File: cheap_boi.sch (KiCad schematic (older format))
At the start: 120 parts, among them SW1 SW_Push, U1 ATmega32U4-AU, Y1 16MHz

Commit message: assigned footprints for all components
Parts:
- MX0, MX0A1, MX0B1, MX0C1, MX1, MX10, MX11, MX12, MX13, MX14, MX15, MX16, MX17, MX18, MX19, MX1A1, MX1B1, MX1C1, MX2, MX20, MX21, MX22, MX23, MX24, MX25, MX26, MX27, MX28, MX29, MX2A1, MX2B1, MX2C1, MX3, MX30, MX31, MX32, MX33, MX34, MX35, MX36, MX37, MX38, MX39, MX3A1, MX3B1, MX3C1, MX4, MX5, MX6, MX7, MX8, MX9: footprint (none) -> MX_Alps_Hybrid_2:MX-1U-NoLED
- R1, R2, R3, R4: footprint (none) -> Resistor_SMD:R_0805_2012Metric
- SW1: footprint (none) -> random-keyboard-parts:SKQG-1155865
- USB1: footprint (none) -> random-keyboard-parts:Molex-0548190589
- Y1: footprint (none) -> Crystal:Crystal_SMD_3225-4Pin_3.2x2.5mm

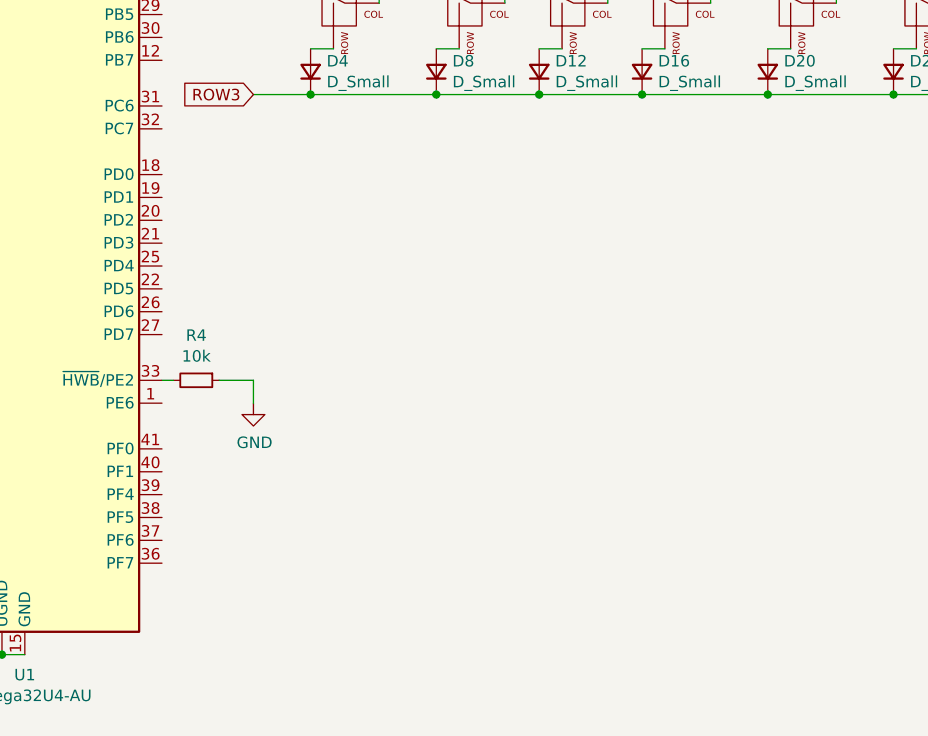
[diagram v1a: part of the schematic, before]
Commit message: added RGB breakout and ordered parts in symmetrically
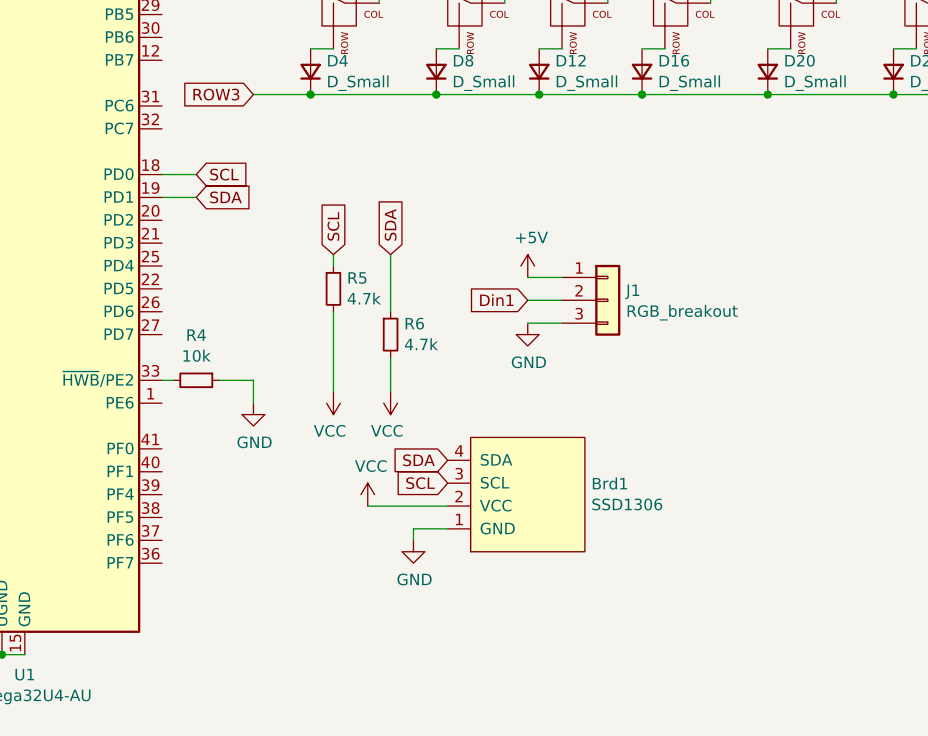
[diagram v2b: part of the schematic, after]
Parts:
- added Brd1: SSD1306, SSD1306:128x64OLED, symbol SSD1306-128x64_OLED:SSD1306
- added J1: RGB_breakout, Connector_PinHeader_1.00mm:PinHeader_1x03_P1.00mm_Vertical_SMD_Pin1Left, symbol Connector_Generic:Conn_01x03
- added R5, R6: 4.7k, Resistor_SMD:R_0805_2012Metric, symbol Device:R_Small
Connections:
- net +5V: now also J1.1 (Pin_1)
- net GND: now also Brd1.1 (GND), J1.3 (Pin_3)
- net VCC: now also Brd1.2 (VCC), R5.2, R6.2
- net SCL: now reaches U1.18 (PD0)
- net SCL: now also Brd1.3 (SCL), R5.1
- net SDA: now reaches U1.19 (PD1)
- net SDA: now also Brd1.4 (SDA), R6.1
- new net Din1: J1.2 (Pin_2)
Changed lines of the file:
@@
 	1    0    0    -1
 $EndComp
+Text GLabel 3400 4900 2    50   Input ~ 0
+SDA
+Text GLabel 3400 4800 2    50   Input ~ 0
+SCL
+Wire Wire Line
+	3250 4800 3400 4800
+Wire Wire Line
+	3400 4900 3250 4900
+$Comp
+L SSD1306-128x64_OLED:SSD1306 Brd1
+U 1 1 5EFF64F3
+P 4850 6200
+F 0 "Brd1" V 4896 5922 50  0000 R CNN
+F 1 "SSD1306" V 4805 5922 50  0000 R CNN
+F 2 "SSD1306:128x64OLED" H 4850 6450 50  0001 C CNN
+F 3 "" H 4850 6450 50  0001 C CNN
+	1    4850 6200
+	0    -1   -1   0
+$EndComp
+Text GLabel 4500 6150 0    50   Input ~ 0
+SCL
+Text GLabel 4500 6050 0    50   Input ~ 0
+SDA
+$Comp
+L power:GND #PWR0114
+U 1 1 5F0207B3
+P 4350 6400
+F 0 "#PWR0114" H 4350 6150 50  0001 C CNN
+F 1 "GND" H 4355 6227 50  0000 C CNN
+F 2 "" H 4350 6400 50  0001 C CNN
+F 3 "" H 4350 6400 50  0001 C CNN
+	1    4350 6400
+	1    0    0    -1
+$EndComp
+Wire Wire Line
+	4500 6350 4350 6350
+Wire Wire Line
+	4350 6350 4350 6400
+Wire Wire Line
+	4500 6250 4150 6250
+$Comp
+L power:VCC #PWR0115
+U 1 1 5F08A572
+P 4150 6250
+F 0 "#PWR0115" H 4150 6100 50  0001 C CNN
+F 1 "VCC" H 4165 6423 50  0000 C CNN
+F 2 "" H 4150 6250 50  0001 C CNN
+F 3 "" H 4150 6250 50  0001 C CNN
+	1    4150 6250
+	1    0    0    -1
+$EndComp
+Text GLabel 4000 5150 1    50   Input ~ 0
+SCL
+Text GLabel 4250 5150 1    50   Input ~ 0
+SDA
+$Comp
+L Device:R_Small R5
+U 1 1 5F0A18D6
+P 4000 5300
+F 0 "R5" H 4059 5346 50  0000 L CNN
+F 1 "4.7k" H 4059 5255 50  0000 L CNN
+F 2 "Resistor_SMD:R_0805_2012Metric" H 4000 5300 50  0001 C CNN
+F 3 "~" H 4000 5300 50  0001 C CNN
+	1    4000 5300
+	1    0    0    -1
+$EndComp
+$Comp
+L Device:R_Small R6
+U 1 1 5F0A2642
+P 4250 5500
+F 0 "R6" H 4309 5546 50  0000 L CNN
+F 1 "4.7k" H 4309 5455 50  0000 L CNN
+F 2 "Resistor_SMD:R_0805_2012Metric" H 4250 5500 50  0001 C CNN
+F 3 "~" H 4250 5500 50  0001 C CNN
+	1    4250 5500
+	1    0    0    -1
+$EndComp
+Wire Wire Line
+	4250 5150 4250 5400
+Wire Wire Line
+	4000 5150 4000 5200
+$Comp
+L power:VCC #PWR0116
+U 1 1 5F0D2F2C
+P 4250 5750
+F 0 "#PWR0116" H 4250 5600 50  0001 C CNN
+F 1 "VCC" H 4265 5923 50  0000 C CNN
+F 2 "" H 4250 5750 50  0001 C CNN
+F 3 "" H 4250 5750 50  0001 C CNN
+	1    4250 5750
+	-1   0    0    1
+$EndComp
+$Comp
+L power:VCC #PWR0117
+U 1 1 5F0D3517
+P 4000 5750
+F 0 "#PWR0117" H 4000 5600 50  0001 C CNN
+F 1 "VCC" H 4015 5923 50  0000 C CNN
+F 2 "" H 4000 5750 50  0001 C CNN
+F 3 "" H 4000 5750 50  0001 C CNN
+	1    4000 5750
+	-1   0    0    1
+$EndComp
+Wire Wire Line
+	4250 5600 4250 5750
+Wire Wire Line
+	4000 5400 4000 5750
+$Comp
+L Connector_Generic:Conn_01x03 J1
+U 1 1 5EF82DD1
+P 5200 5350
+F 0 "J1" H 5280 5392 50  0000 L CNN
+F 1 "RGB_breakout" H 5280 5301 50  0000 L CNN
+F 2 "Connector_PinHeader_1.00mm:PinHeader_1x03_P1.00mm_Vertical_SMD_Pin1Left" H 5200 5350 50  0001 C CNN
+F 3 "~" H 5200 5350 50  0001 C CNN
+	1    5200 5350
+	1    0    0    -1
+$EndComp
+$Comp
+L power:GND #PWR0118
+U 1 1 5F001636
+P 4850 5450
+F 0 "#PWR0118" H 4850 5200 50  0001 C CNN
+F 1 "GND" H 4855 5277 50  0000 C CNN
+F 2 "" H 4850 5450 50  0001 C CNN
+F 3 "" H 4850 5450 50  0001 C CNN
+	1    4850 5450
+	1    0    0    -1
+$EndComp
+$Comp
+L power:+5V #PWR0119
+U 1 1 5F00271B
+P 4850 5250
+F 0 "#PWR0119" H 4850 5100 50  0001 C CNN
+F 1 "+5V" H 4865 5423 50  0000 C CNN
+F 2 "" H 4850 5250 50  0001 C CNN
+F 3 "" H 4850 5250 50  0001 C CNN
+	1    4850 5250
+	1    0    0    -1
+$EndComp
+Text GLabel 4850 5350 0    50   Input ~ 0
+Din1
+Wire Wire Line
+	4850 5250 5000 5250
+Wire Wire Line
+	4850 5350 5000 5350
+Wire Wire Line
+	4850 5450 5000 5450
 $EndSCHEMATC

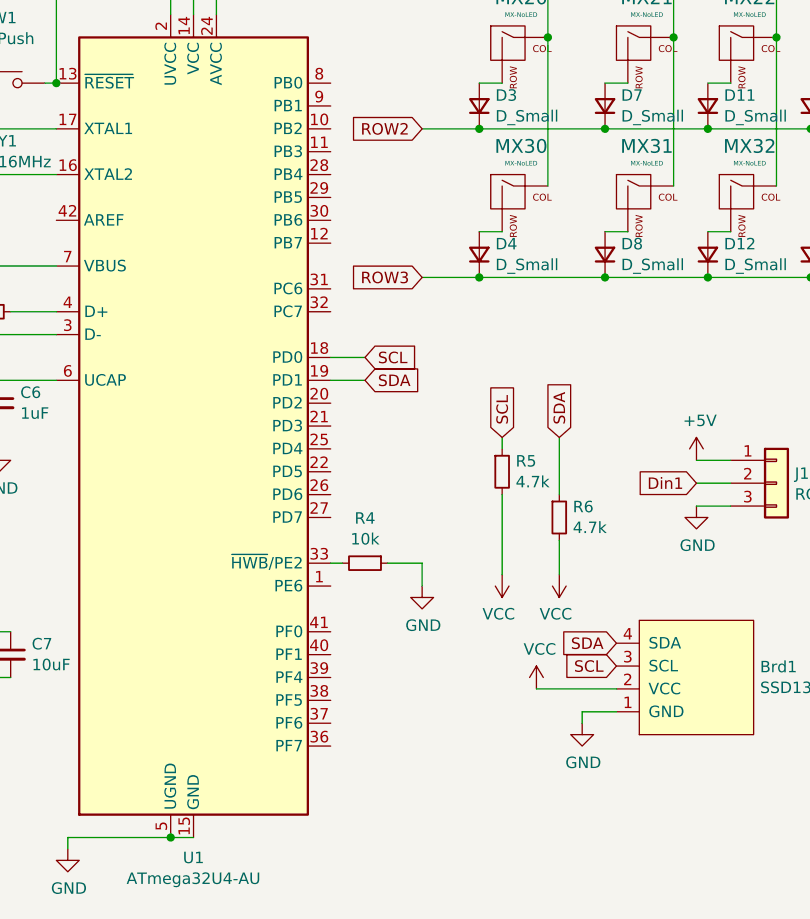
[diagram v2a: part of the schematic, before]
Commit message: added connection of rows and cols to microcontroller
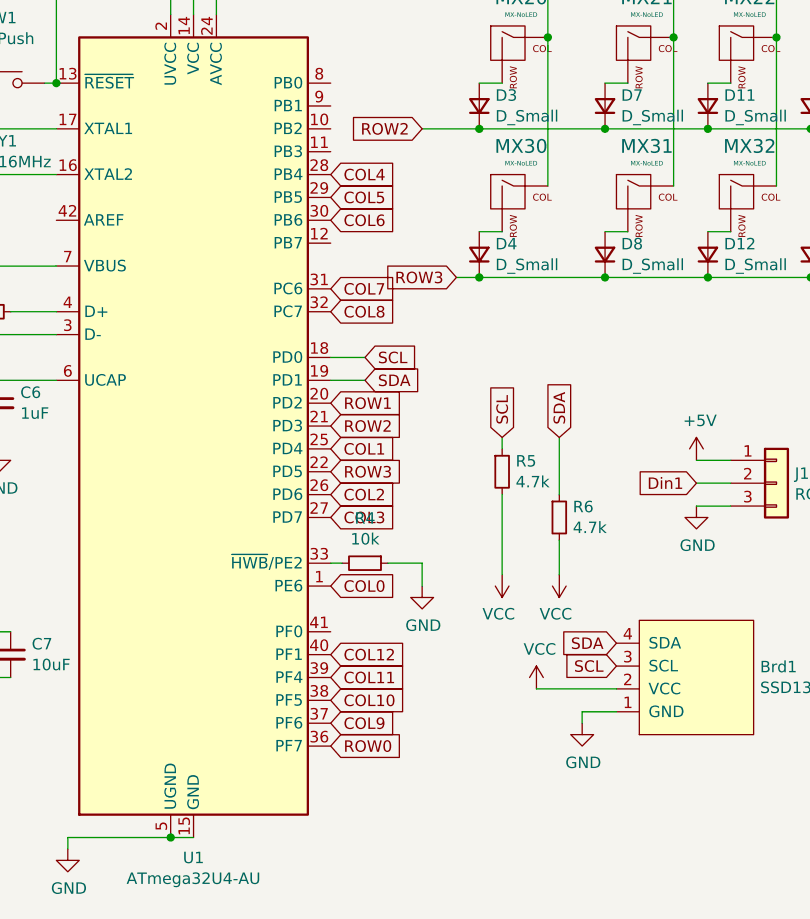
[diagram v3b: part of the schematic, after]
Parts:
- J1: footprint Connector_PinHeader_1.00mm:PinHeader_1x03_P1.00mm_Vertical_SMD_Pin1Left -> Connector_PinHeader_1.00mm:PinHeader_1x03_P1.00mm_Vertical
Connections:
- net COL0: now also U1.1 (PE6)
- net COL1: now also U1.25 (PD4)
- net COL10: now also U1.38 (PF5)
- net COL11: now also U1.39 (PF4)
- net COL12: now also U1.40 (PF1)
- net COL2: now also U1.26 (PD6)
- net COL3: now also U1.27 (PD7)
- net COL4: now also U1.28 (PB4)
- net COL5: now also U1.29 (PB5)
- net COL6: now also U1.30 (PB6)
- net COL7: now also U1.31 (PC6)
- net COL8: now also U1.32 (PC7)
- net COL9: now also U1.37 (PF6)
- net ROW0: now also U1.36 (PF7)
- net ROW1: now also U1.20 (PD2)
- net ROW2: now also U1.21 (PD3)
- net ROW3: now also U1.22 (PD5)
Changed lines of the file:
@@
 Connection ~ 3900 4450
 Wire Wire Line
-	3900 4450 3650 4450
+	3900 4450 3800 4450
 Connection ~ 4450 4450
 Wire Wire Line
@@
 Text GLabel 3650 3800 0    50   Input ~ 0
 ROW2
-Text GLabel 3650 4450 0    50   Input ~ 0
+Text GLabel 3800 4450 0    50   Input ~ 0
 ROW3
 Wire Wire Line
@@
 F 0 "#PWR0116" H 4250 5600 50  0001 C CNN
 F 1 "VCC" H 4265 5923 50  0000 C CNN
-F 2 "" H 4250 5750 50  0001 C CNN
+F 2 "COL6" H 4250 5750 50  0001 C CNN
 F 3 "" H 4250 5750 50  0001 C CNN
 	1    4250 5750
@@
 F 0 "J1" H 5280 5392 50  0000 L CNN
 F 1 "RGB_breakout" H 5280 5301 50  0000 L CNN
-F 2 "Connector_PinHeader_1.00mm:PinHeader_1x03_P1.00mm_Vertical_SMD_Pin1Left" H 5200 5350 50  0001 C CNN
+F 2 "Connector_PinHeader_1.00mm:PinHeader_1x03_P1.00mm_Vertical" H 5200 5350 50  0001 C CNN
 F 3 "~" H 5200 5350 50  0001 C CNN
 	1    5200 5350
@@
 Wire Wire Line
 	4850 5450 5000 5450
+Text GLabel 3250 6500 2    50   Input ~ 0
+ROW0
+Text GLabel 3250 5000 2    50   Input ~ 0
+ROW1
+Text GLabel 3250 5100 2    50   Input ~ 0
+ROW2
+Text GLabel 3250 5300 2    50   Input ~ 0
+ROW3
+Text GLabel 3250 5800 2    50   Input ~ 0
+COL0
+Text GLabel 3250 5200 2    50   Input ~ 0
+COL1
+Text GLabel 3250 5400 2    50   Input ~ 0
+COL2
+Text GLabel 3250 5500 2    50   Input ~ 0
+COL3
+Text GLabel 3250 4000 2    50   Input ~ 0
+COL4
+Text GLabel 3250 4100 2    50   Input ~ 0
+COL5
+Text GLabel 3250 4200 2    50   Input ~ 0
+COL6
+Text GLabel 3250 4500 2    50   Input ~ 0
+COL7
+Text GLabel 3250 4600 2    50   Input ~ 0
+COL8
+Text GLabel 3250 6400 2    50   Input ~ 0
+COL9
+Text GLabel 3250 6300 2    50   Input ~ 0
+COL10
+Text GLabel 3250 6200 2    50   Input ~ 0
+COL11
+Text GLabel 3250 6100 2    50   Input ~ 0
+COL12
 $EndSCHEMATC

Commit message: tracing is done, PCB should be functional
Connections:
- net Din1: now also U1.8 (PB0)
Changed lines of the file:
@@
 Text GLabel 3250 6100 2    50   Input ~ 0
 COL12
+Text GLabel 3250 3600 2    50   Input ~ 0
+Din1
 $EndSCHEMATC

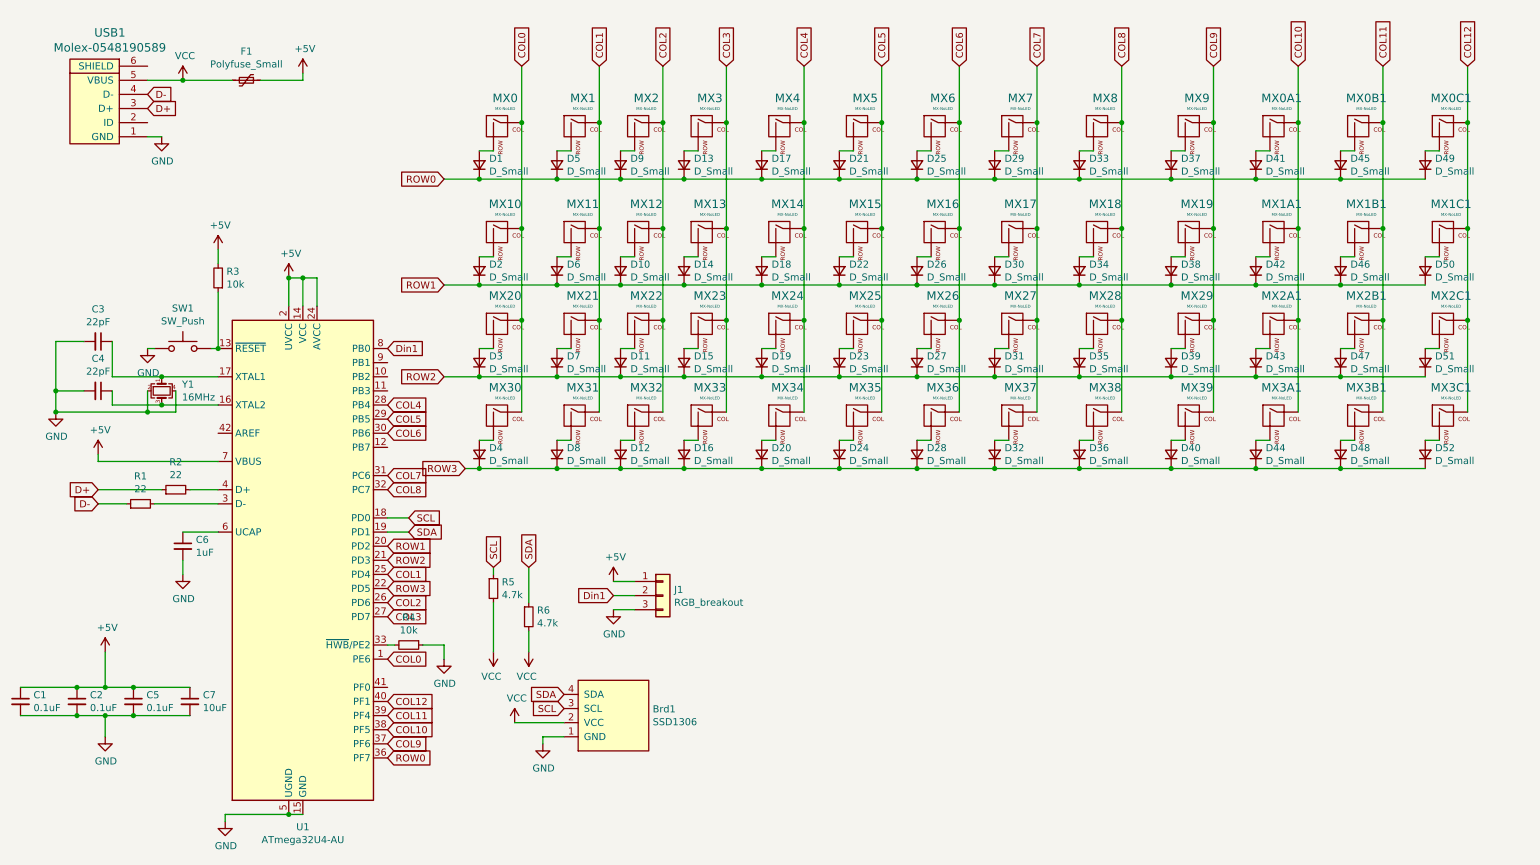
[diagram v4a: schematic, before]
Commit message: added RGB underglow, removed 3 pin breakout for RGB underglow
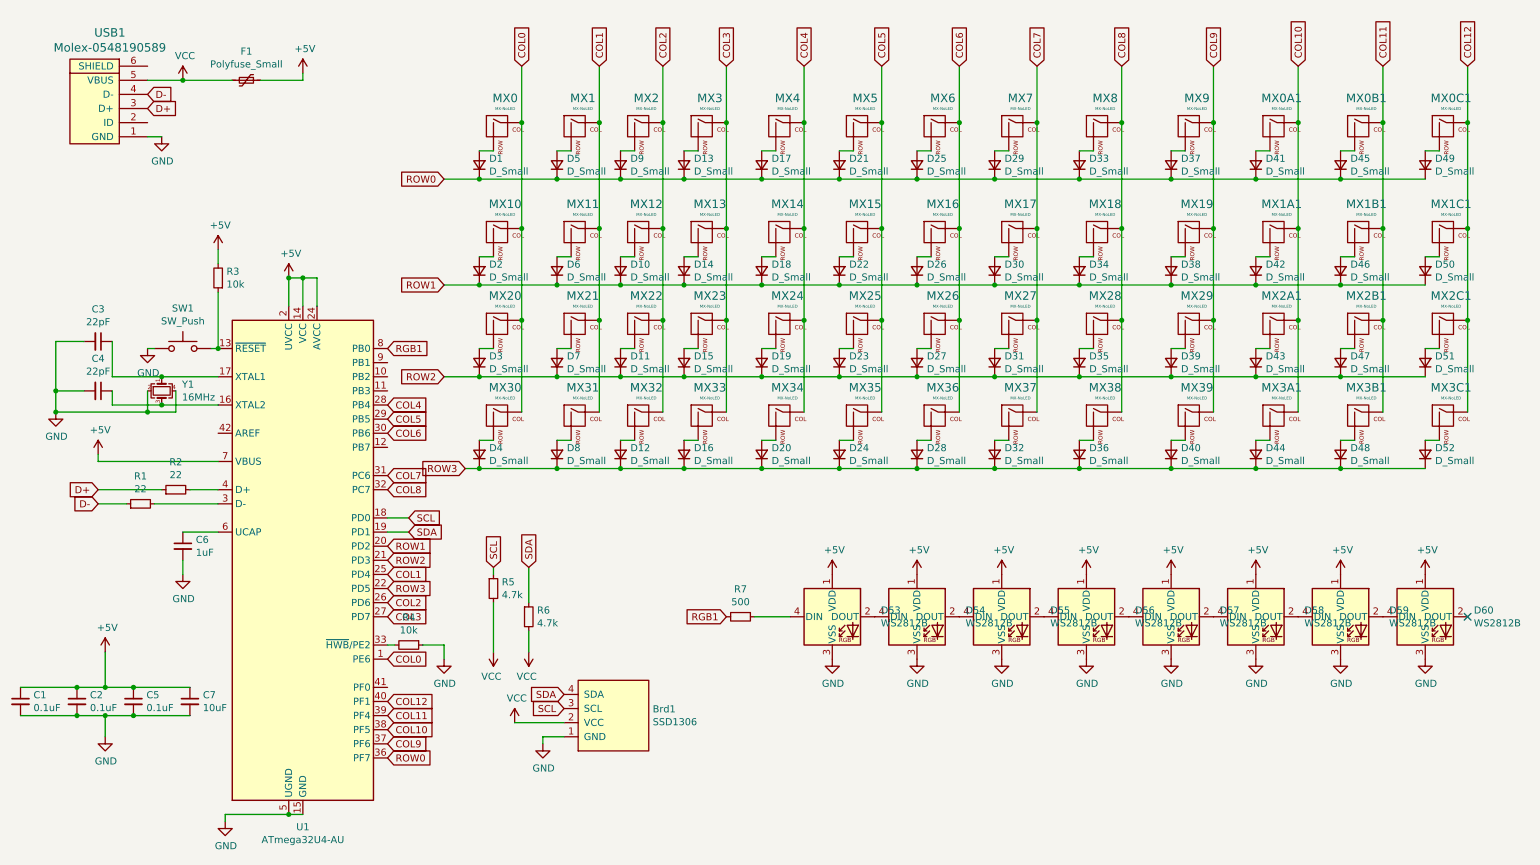
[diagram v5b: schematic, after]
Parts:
- removed J1: RGB_breakout, Connector_PinHeader_1.00mm:PinHeader_1x03_P1.00mm_Vertical, symbol Connector_Generic:Conn_01x03
- added D53, D54, D55, D56, D57, D58, D59, D60: WS2812B, LED_SMD:LED_WS2812B_PLCC4_5.0x5.0mm_P3.2mm, symbol LED:WS2812B
- added R7: 500, Resistor_SMD:R_0805_2012Metric, symbol Device:R_Small
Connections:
- net +5V: now also D53.1 (VDD), D54.1 (VDD), D55.1 (VDD), D56.1 (VDD), D57.1 (VDD), D58.1 (VDD), D59.1 (VDD), D60.1 (VDD)
- net GND: now also D53.3 (VSS), D54.3 (VSS), D55.3 (VSS), D56.3 (VSS), D57.3 (VSS), D58.3 (VSS), D59.3 (VSS), D60.3 (VSS)
- net Din1 renamed RGB1
- net RGB1: now also R7.2
- new net: D53.2 (DOUT), D54.4 (DIN)
- new net: D53.4 (DIN), R7.1
- new net: D54.2 (DOUT), D55.4 (DIN)
- new net: D55.2 (DOUT), D56.4 (DIN)
- new net: D56.2 (DOUT), D57.4 (DIN)
- new net: D57.2 (DOUT), D58.4 (DIN)
- new net: D58.2 (DOUT), D59.4 (DIN)
- new net: D59.2 (DOUT), D60.4 (DIN)
- no-connect marks 0 -> 1

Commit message: add Gerbers + gerber zip
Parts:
- F1: value Polyfuse_Small -> 500mA
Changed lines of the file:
@@
 P 2250 1700
 F 0 "F1" V 2045 1700 50  0000 C CNN
-F 1 "Polyfuse_Small" V 2136 1700 50  0000 C CNN
+F 1 "500mA" V 2136 1700 50  0000 C CNN
 F 2 "Fuse:Fuse_1206_3216Metric" H 2300 1500 50  0001 L CNN
 F 3 "~" H 2250 1700 50  0001 C CNN

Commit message: added new gerbers
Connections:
- net GND: now also USB1.6 (SHIELD)
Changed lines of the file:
@@
 $EndComp
 NoConn ~ 10900 5500
+$Comp
+L power:GND #PWR?
+U 1 1 5EF4216C
+P 1850 1300
+F 0 "#PWR?" H 1850 1050 50  0001 C CNN
+F 1 "GND" H 1855 1127 50  0000 C CNN
+F 2 "" H 1850 1300 50  0001 C CNN
+F 3 "" H 1850 1300 50  0001 C CNN
+	1    1850 1300
+	1    0    0    -1
+$EndComp
+Wire Wire Line
+	1550 1600 1550 1300
+Wire Wire Line
+	1550 1300 1850 1300
 $EndSCHEMATC

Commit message: we are now on rev 1.1, pcbs soon to be tested
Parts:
- added MX40: MX-NoLED, MX_Alps_Hybrid_2:MX-2U-ReversedStabilizers-NoLED, symbol MX_Alps_Hybrid:MX-NoLED
- C1, C2, C3, C4, C5, C6, C7: symbol Device:C_Small -> cheap_boi-rescue:C_Small-Device
- D1, D10, D11, D12, D13, D14, D15, D16, D17, D18, D19, D2, D20, D21, D22, D23, D24, D25, D26, D27, D28, D29, D3, D30, D31, D32, D33, D34, D35, D36, D37, D38, D39, D4, D40, D41, D42, D43, D44, D45, D46, D47, D48, D49, D5, D50, D51, D52, D6, D7, D8, D9: symbol Device:D_Small -> cheap_boi-rescue:D_Small-Device
- D53, D54, D55, D56, D57, D58, D59, D60: symbol LED:WS2812B -> cheap_boi-rescue:WS2812B-LED
- F1: symbol Device:Polyfuse_Small -> cheap_boi-rescue:Polyfuse_Small-Device
- R1, R2, R3, R4, R5, R6, R7: symbol Device:R_Small -> cheap_boi-rescue:R_Small-Device
- SW1: symbol Switch:SW_Push -> cheap_boi-rescue:SW_Push-Switch
- U1: symbol MCU_Microchip_ATmega:ATmega32U4-AU -> cheap_boi-rescue:ATmega32U4-AU-MCU_Microchip_ATmega
- Y1: footprint Crystal:Crystal_SMD_3225-4Pin_3.2x2.5mm -> Crystal:Crystal_SMD_3225-4Pin_3.2x2.5mm_HandSoldering; symbol Device:Crystal_GND24_Small -> cheap_boi-rescue:Crystal_GND24_Small-Device
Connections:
- net COL6: now also MX40.1 (COL)
- net at D28.2 (A), MX36.2 (ROW): now also MX40.2 (ROW)
